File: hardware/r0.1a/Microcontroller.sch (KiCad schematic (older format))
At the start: 71 parts, among them J1 STLink, J2 USB_C, J3 OLED, SW1 Button 1, SW2 Button 2, SW3 Reset, SW4 Rotary, U1 USBLC6-2, U2 W25Q16, U3 STM32F407VETx, U4 LM1117-3.3, Y1 8 MHz

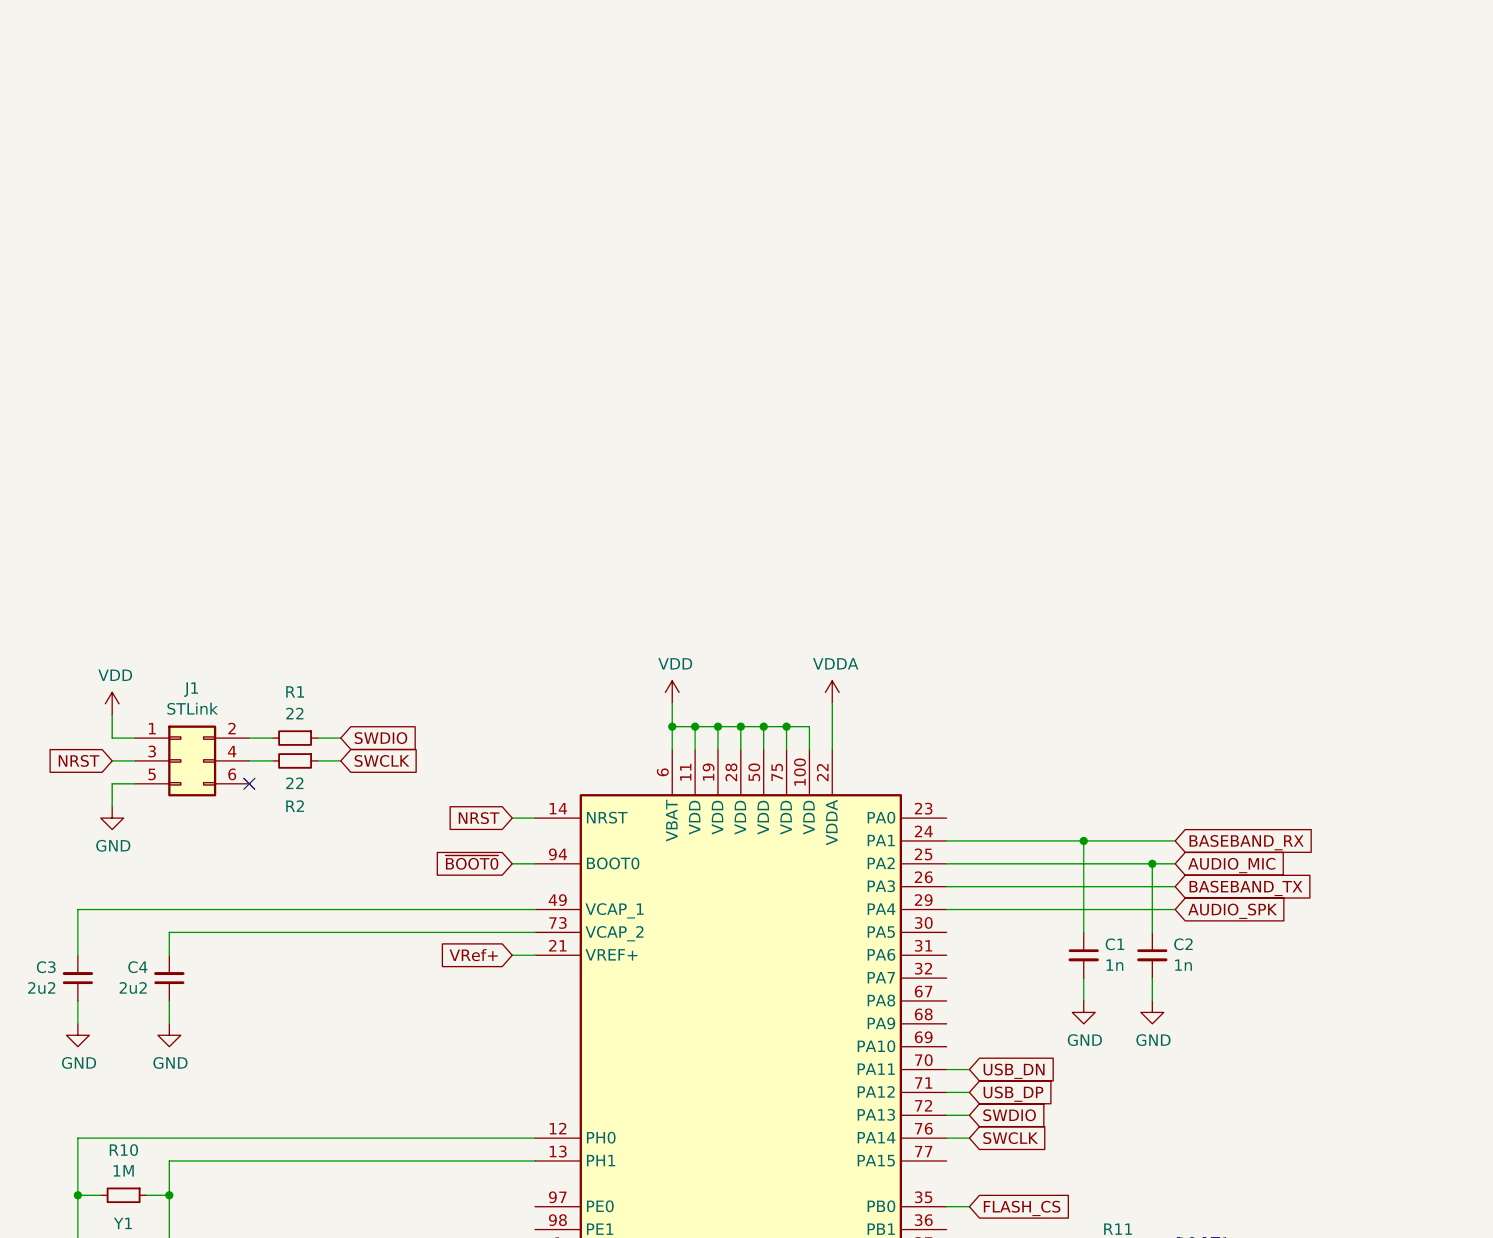
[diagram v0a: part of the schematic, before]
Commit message: Moved DAC signals to DAC channels (PA4/5)
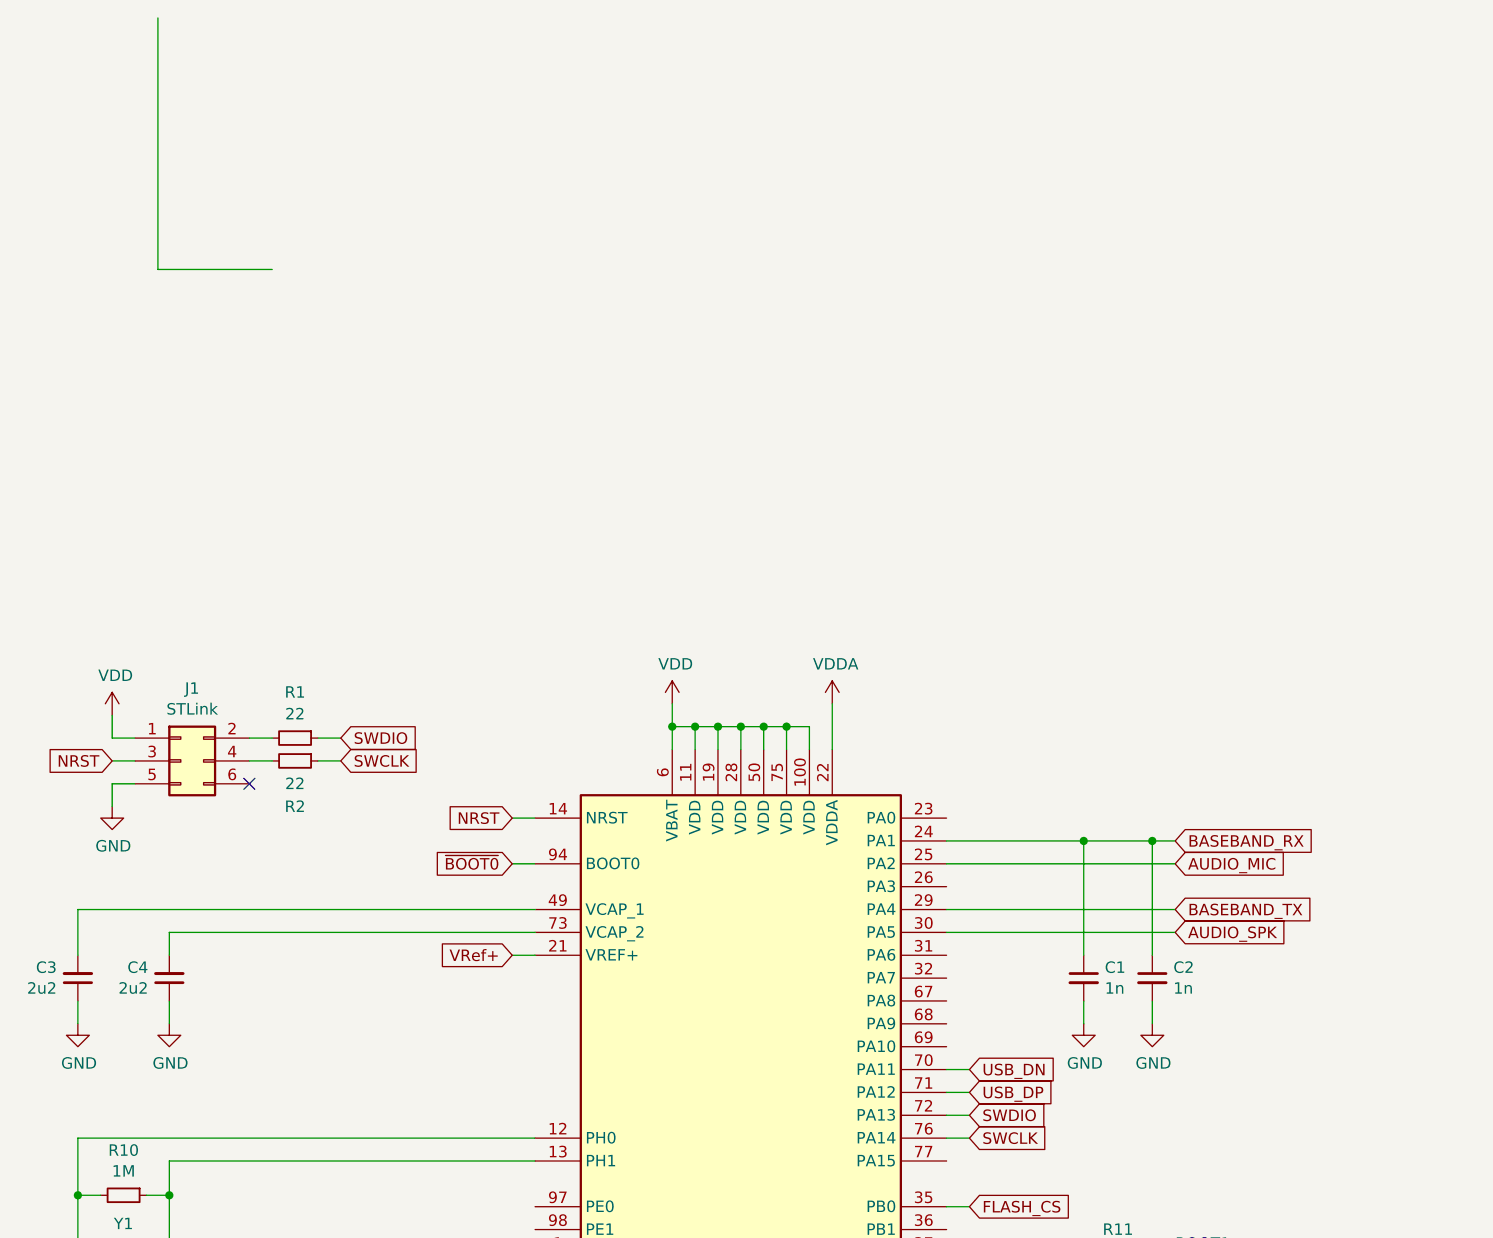
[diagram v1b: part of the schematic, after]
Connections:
- net AUDIO_MIC: no longer C2.1
- net AUDIO_SPK: now also U3.30 (PA5); no longer U3.29 (PA4)
- net BASEBAND_RX: now also C2.1
- net BASEBAND_TX: now also U3.29 (PA4); no longer U3.26 (PA3)
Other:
- moved on the sheet: C1, C2
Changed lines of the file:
@@
 L pkl_device:pkl_C_Small C1
 U 1 1 61D3DBC5
-P 5250 1950
-F 0 "C1" H 5342 1996 50  0000 L CNN
-F 1 "1n" H 5342 1905 50  0000 L CNN
-F 2 "" H 5250 1950 60  0000 C CNN
-F 3 "" H 5250 1950 60  0000 C CNN
-	1    5250 1950
+P 5250 2050
+F 0 "C1" H 5342 2096 50  0000 L CNN
+F 1 "1n" H 5342 2005 50  0000 L CNN
+F 2 "" H 5250 2050 60  0000 C CNN
+F 3 "" H 5250 2050 60  0000 C CNN
+	1    5250 2050
 	1    0    0    -1
 $EndComp
@@
 L pkl_device:pkl_C_Small C2
 U 1 1 61D4265E
-P 5550 1950
-F 0 "C2" H 5642 1996 50  0000 L CNN
-F 1 "1n" H 5642 1905 50  0000 L CNN
-F 2 "" H 5550 1950 60  0000 C CNN
-F 3 "" H 5550 1950 60  0000 C CNN
-	1    5550 1950
+P 5550 2050
+F 0 "C2" H 5642 2096 50  0000 L CNN
+F 1 "1n" H 5642 2005 50  0000 L CNN
+F 2 "" H 5550 2050 60  0000 C CNN
+F 3 "" H 5550 2050 60  0000 C CNN
+	1    5550 2050
 	1    0    0    -1
 $EndComp
 Wire Wire Line
-	4650 1450 5250 1450
+	4650 1750 5650 1750
 Wire Wire Line
-	5250 1450 5250 1850
-Wire Wire Line
-	4650 1550 5550 1550
-Wire Wire Line
-	5550 1550 5550 1850
-Wire Wire Line
-	5250 1450 5650 1450
-Connection ~ 5250 1450
-Wire Wire Line
-	5550 1550 5650 1550
-Connection ~ 5550 1550
-Wire Wire Line
-	4650 1650 5650 1650
-Wire Wire Line
-	4650 1750 5650 1750
+	4650 1850 5650 1850
 $Comp
 L power:GND #PWR010
 U 1 1 61DA70B6
-P 5250 2150
-F 0 "#PWR010" H 5250 1900 50  0001 C CNN
-F 1 "GND" H 5255 1977 50  0000 C CNN
-F 2 "" H 5250 2150 50  0001 C CNN
-F 3 "" H 5250 2150 50  0001 C CNN
-	1    5250 2150
+P 5250 2250
+F 0 "#PWR010" H 5250 2000 50  0001 C CNN
+F 1 "GND" H 5255 2077 50  0000 C CNN
+F 2 "" H 5250 2250 50  0001 C CNN
+F 3 "" H 5250 2250 50  0001 C CNN
+	1    5250 2250
 	1    0    0    -1
 $EndComp
@@
 L power:GND #PWR011
 U 1 1 61DA895F
-P 5550 2150
-F 0 "#PWR011" H 5550 1900 50  0001 C CNN
-F 1 "GND" H 5555 1977 50  0000 C CNN
-F 2 "" H 5550 2150 50  0001 C CNN
-F 3 "" H 5550 2150 50  0001 C CNN
-	1    5550 2150
+P 5550 2250
+F 0 "#PWR011" H 5550 2000 50  0001 C CNN
+F 1 "GND" H 5555 2077 50  0000 C CNN
+F 2 "" H 5550 2250 50  0001 C CNN
+F 3 "" H 5550 2250 50  0001 C CNN
+	1    5550 2250
 	1    0    0    -1
 $EndComp
 Wire Wire Line
-	5550 2050 5550 2150
+	5550 2150 5550 2250
 Wire Wire Line
-	5250 2050 5250 2150
+	5250 2150 5250 2250
 Text GLabel 5650 1450 2    50   Input ~ 0
 BASEBAND_RX
 Text GLabel 5650 1550 2    50   Input ~ 0
 AUDIO_MIC
-Text GLabel 5650 1650 2    50   Input ~ 0
+Text GLabel 5650 1750 2    50   Input ~ 0
 BASEBAND_TX
-Text GLabel 5650 1750 2    50   Input ~ 0
+Text GLabel 5650 1850 2    50   Input ~ 0
 AUDIO_SPK
 Wire Wire Line
@@
 Wire Wire Line
 	2850 4550 2750 4550
+Wire Wire Line
+	4650 1450 5250 1450
+Wire Wire Line
+	4650 1550 5650 1550
+Wire Wire Line
+	1200 -2150 1200 -1050
+Wire Wire Line
+	1200 -1050 1700 -1050
+Wire Wire Line
+	5250 1950 5250 1450
+Connection ~ 5250 1450
+Wire Wire Line
+	5250 1450 5550 1450
+Wire Wire Line
+	5550 1950 5550 1450
+Connection ~ 5550 1450
+Wire Wire Line
+	5550 1450 5650 1450
 $EndSCHEMATC

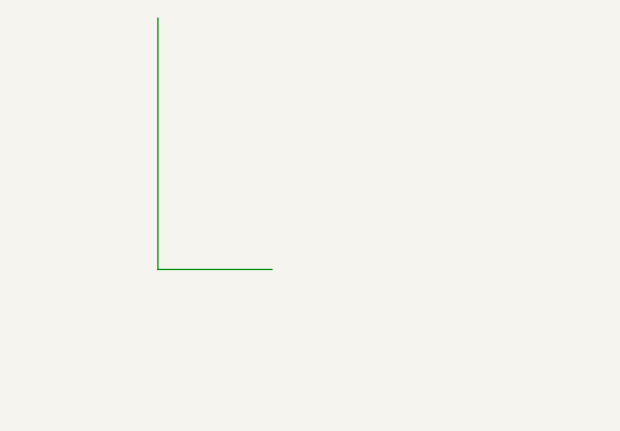
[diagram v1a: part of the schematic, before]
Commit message: Simplified values of R32 and C46,47
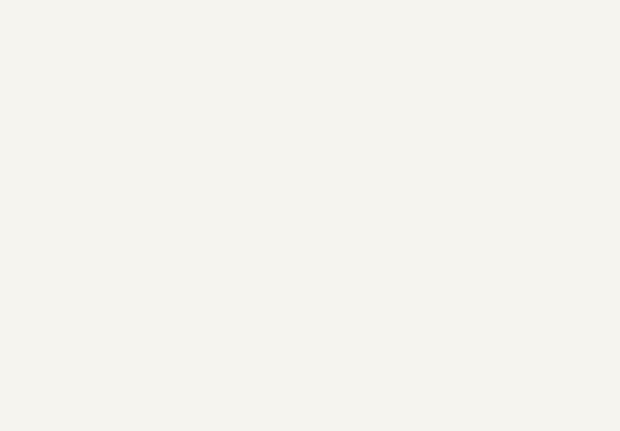
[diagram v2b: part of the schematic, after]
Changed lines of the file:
@@
 	4650 1550 5650 1550
-Wire Wire Line
-	1200 -2150 1200 -1050
-Wire Wire Line
-	1200 -1050 1700 -1050
 Wire Wire Line
 	5250 1950 5250 1450
